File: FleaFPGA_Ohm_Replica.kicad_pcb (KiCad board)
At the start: 4 copper layers, 65 x 30 mm, 122 parts, among them J301 HDMI_C_1.3, J401 JTAG, J402 USB_B_Micro, J403 Conn_02x20, J404 Micro_SD_Card_Det2, J405 USB1, J406 USB2, U201 LFE5U-25F-6BGA256C, U401 FT230XQ, U402 MT48LC16M16A2, U403 MX25L1606, U404 TPD4E02B04DQA, U405 AP3417C, U406 AP3417C, U407 AP3417C, X401 XO32

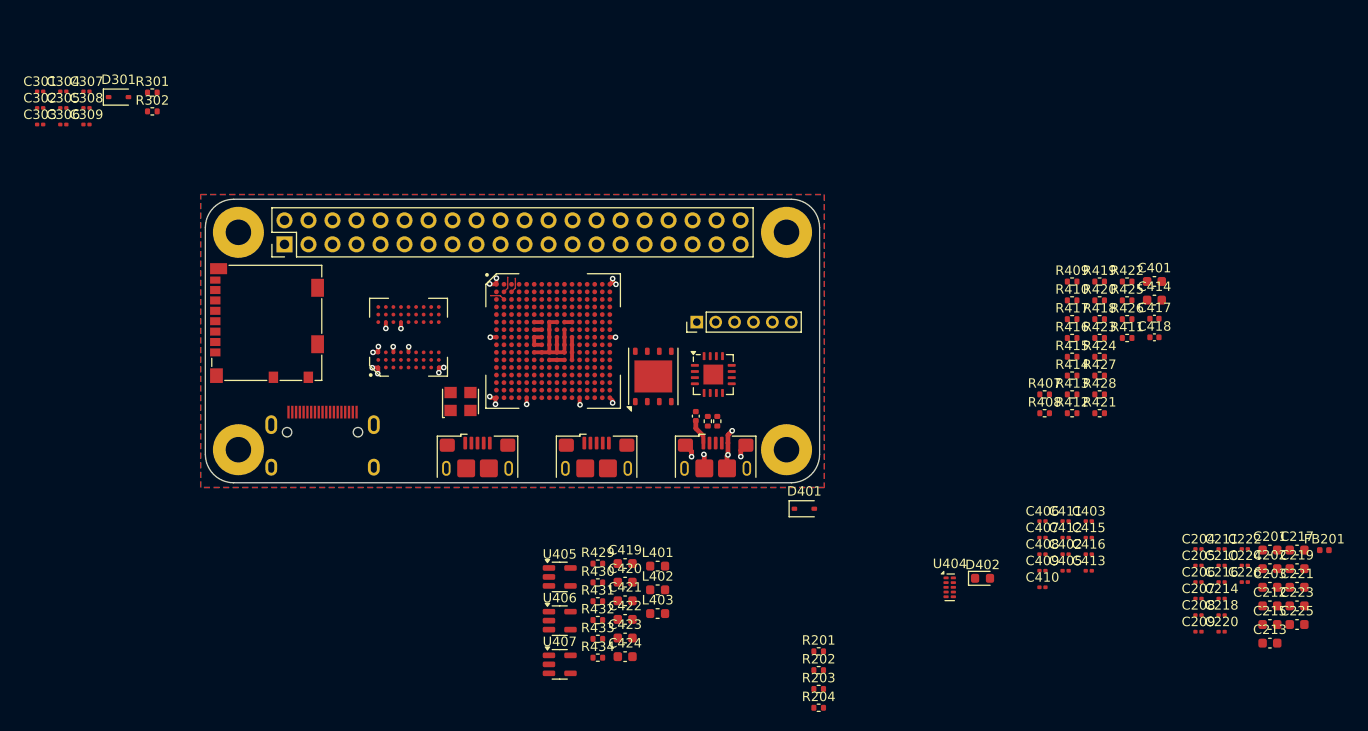
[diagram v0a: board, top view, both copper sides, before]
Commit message: Towards routing RAM
 - Moved the RAM to its own sheet
 - Use the ECP5 prefix to capture impedance controlled traces
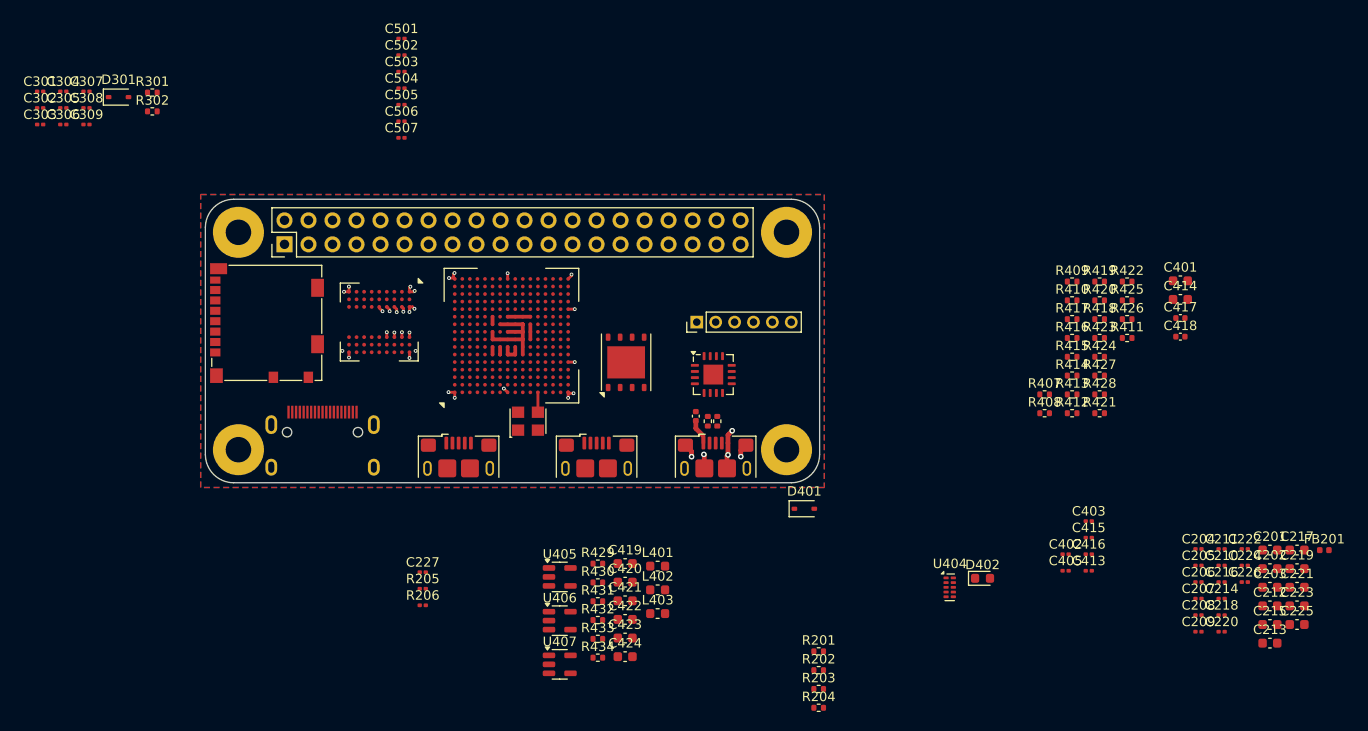
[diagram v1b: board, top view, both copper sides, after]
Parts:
- removed C406, C407, C408, C409, C410, C411, C412: 100n, Capacitor_SMD:C_0201_0603Metric
- removed U402: MT48LC16M16A2, Package_BGA_Extra:Micron_VFBGA-64_8.0x8.0mm_Layout9x9_P0.8mm
- added C227: 100n, Capacitor_SMD:C_0201_0603Metric, F.Cu at (123.0, 119.5)
- added C501: 100n, Capacitor_SMD:C_0201_0603Metric, F.Cu at (120.8, 63.0)
- added C502: 100n, Capacitor_SMD:C_0201_0603Metric, F.Cu at (120.8, 64.8)
- added C503: 100n, Capacitor_SMD:C_0201_0603Metric, F.Cu at (120.8, 66.5)
- added C504: 100n, Capacitor_SMD:C_0201_0603Metric, F.Cu at (120.8, 68.2)
- added C505: 100n, Capacitor_SMD:C_0201_0603Metric, F.Cu at (120.8, 70.0)
- added C506: 100n, Capacitor_SMD:C_0201_0603Metric, F.Cu at (120.8, 71.8)
- added C507: 100n, Capacitor_SMD:C_0201_0603Metric, F.Cu at (120.8, 73.5)
- added R205: 10k, Resistor_SMD:R_0201_0603Metric, F.Cu at (123.0, 121.2)
- added R206: 10k, Resistor_SMD:R_0201_0603Metric, F.Cu at (123.0, 123.0)
- added U501: MT48LC16M16A2, Package_BGA_Extra:Micron_VFBGA-64_8.0x8.0mm_Layout9x9_P0.8mm, F.Cu at (118.4, 93.0)
- moved X401 7.44 mm to (134.1, 103.5)
- moved U201 4.45 mm to (132.4, 94.4), turned to 90 degrees
- moved U403 3.24 mm to (144.5, 97.3)
- moved C401 2.75 mm to (203.2, 88.6)
- moved C414 2.75 mm to (203.2, 90.6)
- moved C417 2.75 mm to (203.2, 92.6)
- moved C418 2.75 mm to (203.2, 94.5)
- moved J406 2.00 mm to (126.8, 108.5)
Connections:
- U201 pad A10: unconnected-(U201A-PT42B-PadA10) -> /ECP5 FPGA/~{CAS}
- U201 pad A11: unconnected-(U201A-PT53A-PadA11) -> /ECP5 FPGA/BA1
- U201 pad A12: unconnected-(U201A-PT53B-PadA12) -> /ECP5 FPGA/BA0
- U201 pad A13: unconnected-(U201A-PT65A-PadA13) -> /ECP5 FPGA/CKE
- U201 pad A14: unconnected-(U201A-PT65B-PadA14) -> /ECP5 FPGA/CLK
- U201 pad A15: unconnected-(U201A-PT67B-PadA15) -> /ECP5 FPGA/UDQM
- U201 pad A9: unconnected-(U201A-PT42A-PadA9) -> /ECP5 FPGA/~{RAS}
- U201 pad L1: unconnected-(U201B-PL26A-PadL1) -> CK+
- U201 pad L2: unconnected-(U201B-PL26B-PadL2) -> CK-
- U201 pad M1: unconnected-(U201B-PL26C-PadM1) -> SYSCLK
- U201 pad N10: unconnected-(U201B-CFG_0-PadN10) -> GND
- U201 pad N9: unconnected-(U201B-CCLK-PadN9) -> ROM_CLK
- U201 pad P10: unconnected-(U201B-CFG_1-PadP10) -> Net-(U201B-CFG_1)
- U201 pad R10: unconnected-(U201B-CFG_2-PadR10) -> GND
- U201 pad R9: unconnected-(U201B-PROGRAMN-PadR9) -> Net-(U201B-PROGRAMN)
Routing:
- net +3V3: track 6.40 -> 9.76 mm, vias 0 -> 6
- net SYSCLK: track 0.00 -> 2.11 mm
- net unconnected-(U201B-PL2B-PadB2): track 1.71 -> 0.00 mm
- net unconnected-(U201A-PT4B-PadB3): track 1.60 -> 0.00 mm
- net unconnected-(U201B-PL5B-PadC2): track 1.56 -> 0.00 mm
- net GND: track 33.7 -> 32.5 mm, vias 26 -> 28
- removed copper zone on In1.Cu, net GND
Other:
- rule pad_to_mask_clearance: 0 -> 0.038

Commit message: First whole routing
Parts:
- removed C207, C208, C209, C220, C505, C506, C507: 100n, Capacitor_SMD:C_0201_0603Metric
- removed C215, C221, C225, C420, C422, C424: 10u, Capacitor_SMD:C_0603_1608Metric
- removed C421, C423: 4.7u, Capacitor_SMD:C_0603_1608Metric
- removed J401: JTAG, Connector_PinHeader_2.00mm:PinHeader_1x06_P2.00mm_Vertical
- removed J406: USB2, Connector_USB:USB_Micro-B_Amphenol_10118193-0001LF_Horizontal
- removed R201, R202, R203, R204: 4.7k, Resistor_SMD:R_0402_1005Metric
- removed R431: 320k, Resistor_SMD:R_0402_1005Metric
- removed R432, R434: 100k, Resistor_SMD:R_0402_1005Metric
- removed R433: 82k, Resistor_SMD:R_0402_1005Metric
- removed U407: AP3417C, Package_TO_SOT_SMD:SOT-23-5
- removed U501: MT48LC16M16A2, Package_BGA_Extra:Micron_VFBGA-64_8.0x8.0mm_Layout9x9_P0.8mm
- added C406: 4.7uF, Capacitor_SMD:C_0603_1608Metric, B.Cu at (163.4, 90.7)
- added C407: 22uF, Capacitor_SMD:C_0603_1608Metric, B.Cu at (158.8, 90.7)
- added C408: 4.7uF, Capacitor_SMD:C_0603_1608Metric, F.Cu at (163.6, 90.2)
- added C409: 22uF, Capacitor_SMD:C_0603_1608Metric, F.Cu at (159.1, 90.3)
- added C410: 4.7uF, Capacitor_SMD:C_0603_1608Metric, F.Cu at (155.2, 90.3)
- added C411: 10uF, Capacitor_SMD:C_0603_1608Metric, F.Cu at (150.5, 90.4)
- added C412: 22uF, Capacitor_SMD:C_0603_1608Metric, F.Cu at (157.6, 90.3)
- added D403: LED_Small, LED_SMD:LED_0603_1608Metric, F.Cu at (127.3, 106.2)
- added R401: 200k, Resistor_SMD:R_0402_1005Metric, B.Cu at (161.4, 87.9)
- added R402: 100k, Resistor_SMD:R_0402_1005Metric, B.Cu at (161.4, 88.9)
- added R403: 82.5k, Resistor_SMD:R_0402_1005Metric, F.Cu at (161.7, 93.2)
- added R405: 100k, Resistor_SMD:R_0402_1005Metric, F.Cu at (161.7, 92.1)
- added U1: TPD2EUSB30, Package_TO_SOT_SMD:Texas_DRT-3, F.Cu at (141.1, 101.1)
- added U2: ~, Package_BGA_Extra:FBGA-25_8x6mm_Layout5x5_P1mm, F.Cu at (119.5, 91.4)
- added U402: TLV62569DRL, Package_TO_SOT_SMD:SOT-563, B.Cu at (161.2, 90.7)
- C201, C202, C203, C212, C213, C217, C219, C223: footprint Capacitor_SMD:C_0603_1608Metric -> Capacitor_SMD:C_0402_1005Metric; moved to B.Cu
- C204, C205, C206, C210, C211, C214, C216, C218, C222, C224, C226, C227, C414, C415, FB201, R205, R206, R301, R302, R412, R413, R414, R415, R416, R417: moved to B.Cu
- C403: footprint Capacitor_SMD:C_0201_0603Metric -> Capacitor_SMD:C_0603_1608Metric; moved to B.Cu
- C417: footprint Capacitor_SMD:C_0402_1005Metric -> Capacitor_SMD:C_0603_1608Metric; moved to B.Cu
- C418: value 1u -> 1uF; moved to B.Cu
- C419: value 4.7u -> 1uF; footprint Capacitor_SMD:C_0603_1608Metric -> Capacitor_SMD:C_0402_1005Metric; moved to B.Cu
- C501, C502, C503: footprint Capacitor_SMD:C_0201_0603Metric -> Capacitor_SMD:C_0402_1005Metric; moved to B.Cu
- C504: value 100n -> 10u; footprint Capacitor_SMD:C_0201_0603Metric -> Capacitor_SMD:C_0402_1005Metric; moved to B.Cu
- L401: footprint Inductor_SMD:L_0603_1608Metric -> Inductor_SMD:L_0805_2012Metric; moved to B.Cu
- L402, L403: footprint Inductor_SMD:L_0603_1608Metric -> Inductor_SMD:L_0805_2012Metric
- R407: value 820 -> 450k
- R408: value 820 -> 100k
- R409: value 820 -> 330k; footprint Resistor_SMD:R_0402_1005Metric -> Resistor_SMD:R_0603_1608Metric; moved to B.Cu
- R410: value 820 -> 100k; moved to B.Cu
- R425: value 15k -> 22k; moved to B.Cu
- R426: value 15k -> 10k
- R427, R428: value 180 -> 10k
- R429: value 450k -> 10k
- R430: value 100k -> 180
- U403: footprint Package_SON:WSON-8-1EP_6x5mm_P1.27mm_EP3.4x4mm -> Package_SO_Extra:SOP-8-1EP_3.9x4.9mm_P1.27m_EP4.1x3.5mm
- U404: value TPD4E02B04DQA -> TLV62569DRL; footprint Package_SON:USON-10_2.5x1.0mm_P0.5mm -> Package_TO_SOT_SMD:SOT-563
- U405: value AP3417C -> TLV62569DRL; footprint Package_TO_SOT_SMD:SOT-23-5 -> Package_TO_SOT_SMD:SOT-563
- U406: value AP3417C -> TLV75801PDRV; footprint Package_TO_SOT_SMD:SOT-23-5 -> Package_SON:WSON-6-1EP_2x2mm_P0.65mm_EP1x1.6mm; moved to B.Cu
- moved C414 95.7 mm to (107.5, 92.4)
- moved C213 91.2 mm to (128.1, 92.7), turned to 180 degrees
- moved C415 91.0 mm to (105.6, 92.3), turned to 90 degrees
- moved C217 89.1 mm to (128.8, 96.4), turned to -135 degrees
- moved R413 89.0 mm to (103.7, 88.0), turned to -90 degrees
- moved R414 88.5 mm to (103.7, 90.1), turned to 90 degrees
- moved R417 88.3 mm to (103.5, 96.4), turned to -90 degrees
- moved R415 88.1 mm to (103.7, 93.5), turned to -90 degrees
- moved C403 87.4 mm to (110.2, 87.4), turned to 180 degrees
- moved C219 87.3 mm to (132.8, 91.2), turned to 180 degrees
- moved C202 87.1 mm to (129.2, 94.2), turned to -90 degrees
- moved R416 87.0 mm to (104.8, 95.3), turned to 90 degrees
- moved C223 85.9 mm to (133.6, 97.3), turned to -90 degrees
- moved R412 84.2 mm to (107.7, 97.0), turned to 180 degrees
- moved C201 83.6 mm to (131.3, 97.7)
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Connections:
- net /Peripherals/3V3OUT renamed /Peripherals and Power/3V3OUT
- net /Peripherals/USB_CONN_D+ renamed /Peripherals and Power/USB_CONN_D+
- net /Peripherals/USB_CONN_D- renamed /Peripherals and Power/USB_CONN_D-
- net /Peripherals/USB_D+ renamed /Peripherals and Power/USB_D+
- net /Peripherals/USB_D- renamed /Peripherals and Power/USB_D-
- net /Peripherals/VBUS renamed /Peripherals and Power/VBUS
- net Net-(C210-Pad1) renamed /ECP5 FPGA/VCCAUX
- net Net-(J301-CK+) renamed /Video out interface/CONN_HDMI_CLK+
- net Net-(J301-CK-) renamed /Video out interface/CONN_HDMI_CLK-
- net Net-(J301-D0+) renamed /Video out interface/CONN_HDMI_D0+
- net Net-(J301-D0-) renamed /Video out interface/CONN_HDMI_D0-
- net Net-(J301-D1+) renamed /Video out interface/CONN_HDMI_D1+
- net Net-(J301-D1-) renamed /Video out interface/CONN_HDMI_D1-
- net Net-(J301-D2+) renamed /Video out interface/CONN_HDMI_D2+
- net Net-(J301-D2-) renamed /Video out interface/CONN_HDMI_D2-
- net Net-(J301-SCL) renamed /Video out interface/HDMI_SCL
- net Net-(J301-SDA) renamed /Video out interface/HDMI_SDA
- net Net-(J405-D+) renamed /Peripherals and Power/USB1_CONN_DP
- net Net-(J405-D-) renamed /Peripherals and Power/USB1_CONN_DN
- net Net-(U201B-CFG_1) renamed /ECP5 FPGA/CFG_1
- net Net-(U201B-PROGRAMN) renamed /ECP5 FPGA/PROGRAMN
- net Net-(U403-HOLD#) renamed /Peripherals and Power/~{HOLD}
- net Net-(U403-WP#) renamed /Peripherals and Power/~{WP}
- C213 pad 1: +3V3 -> +1V8
- C214 pad 1: +3V3 -> +1V8
- C302 pad 1: CK- -> HDMI_CK-
- C303 pad 1: CK+ -> HDMI_CK+
- C304 pad 1: D0- -> HDMI_D0-
- C305 pad 1: D0+ -> HDMI_D0+
- C306 pad 1: D1- -> HDMI_D1-
- C307 pad 1: D1+ -> HDMI_D1+
- C308 pad 1: D2- -> HDMI_D2-
- C309 pad 1: D2+ -> HDMI_D2+
- C418 pad 1: +5V -> +3V3
- C419 pad 1: +5V -> +2V5
- C501 pad 1: +3V3 -> +1V8
- C502 pad 1: +3V3 -> +1V8
- C503 pad 1: +3V3 -> +1V8
- C504 pad 1: +3V3 -> +1V8
- L401 pad 1: Net-(U405-LX) -> /Peripherals and Power/SW1
- L401 pad 2: +3V3 -> +1V8
- L402 pad 1: Net-(U407-LX) -> /Peripherals and Power/SW2
- L403 pad 1: Net-(U406-LX) -> /Peripherals and Power/SW3
- L403 pad 2: +2V5 -> +3V3
- R407 pad 1: JTAG_TDO -> +3V3
- R407 pad 2: FTJTAG_TDO -> /Peripherals and Power/FB3
- R408 pad 1: JTAG_TDI -> /Peripherals and Power/FB3
- R408 pad 2: FJTAG_TDI -> GND
- R409 pad 1: JTAG_TMS -> +2V5
- R409 pad 2: FJTAG_TMS -> Net-(R409-Pad2)
- R410 pad 1: JTAG_TCK -> /Peripherals and Power/FB4
- R410 pad 2: FJTAG_TCK -> GND
- R423 pad 2: /Peripherals/USB1_CONN_DP -> USB1_DP
- R424 pad 2: /Peripherals/USB1_CONN_DN -> USB1_DN
- R425 pad 1: Net-(J406-D+) -> Net-(R409-Pad2)
- R425 pad 2: USB2_SEL -> /Peripherals and Power/FB4
- R426 pad 1: Net-(J406-D-) -> +3V3
- R426 pad 2: USB2_SEL -> JTAG_TDO
- R427 pad 1: Net-(J406-D+) -> +3V3
- R427 pad 2: /Peripherals/USB2_CONN_DP -> JTAG_TDI
- R428 pad 1: Net-(J406-D-) -> JTAG_TCK
- R428 pad 2: /Peripherals/USB2_CONN_DN -> GND
- R429 pad 2: Net-(U405-FB) -> JTAG_TMS
- R430 pad 1: Net-(U405-FB) -> GND
- R430 pad 2: GND -> Net-(D403-K)
- U201 pad A10: /ECP5 FPGA/~{CAS} -> unconnected-(U201A-PT42B-PadA10)
- U201 pad A11: /ECP5 FPGA/BA1 -> /ECP5 FPGA/DQ7
- U201 pad A12: /ECP5 FPGA/BA0 -> /ECP5 FPGA/DQ0
- U201 pad A13: /ECP5 FPGA/CKE -> /ECP5 FPGA/RWDS
- U201 pad A14: /ECP5 FPGA/CLK -> /ECP5 FPGA/DQ3
- U201 pad A15: /ECP5 FPGA/UDQM -> /ECP5 FPGA/DQ2
- U201 pad A2: unconnected-(U201A-PT4A-PadA2) -> HDMI_D2+
- U201 pad A3: unconnected-(U201A-PT6A-PadA3) -> HDMI_D1+
- U201 pad A4: unconnected-(U201A-PT6B-PadA4) -> HDMI_D1-
- U201 pad A5: unconnected-(U201A-PT18A-PadA5) -> HDMI_D0+
- U201 pad A6: unconnected-(U201A-PT18B-PadA6) -> HDMI_D0-
- U201 pad A7: unconnected-(U201A-PT29A-PadA7) -> HDMI_CK+
- U201 pad A8: unconnected-(U201A-PT29B-PadA8) -> HDMI_CK-
- U201 pad A9: /ECP5 FPGA/~{RAS} -> unconnected-(U201A-PT42A-PadA9)
- U201 pad B1: unconnected-(U201B-PL2A-PadB1) -> SD_DAT2
- U201 pad B11: unconnected-(U201A-PT49A-PadB11) -> /ECP5 FPGA/DQ1
- U201 pad B13: unconnected-(U201A-PT60A-PadB13) -> /ECP5 FPGA/DQ6
- U201 pad B14: unconnected-(U201A-PT67A-PadB14) -> /ECP5 FPGA/DQ4
- U201 pad B15: unconnected-(U201A-PR2B-PadB15) -> GPIO8
- U201 pad B16: unconnected-(U201A-PR2A-PadB16) -> GPIO9
- U201 pad B2: unconnected-(U201B-PL2B-PadB2) -> SD_CS
- U201 pad B3: unconnected-(U201A-PT4B-PadB3) -> HDMI_D2-
- U201 pad B8: unconnected-(U201A-PT35B-PadB8) -> /ECP5 FPGA/CK_P
- U201 pad C1: unconnected-(U201B-PL5A-PadC1) -> SD_DET
- U201 pad C13: unconnected-(U201A-PT60B-PadC13) -> /ECP5 FPGA/DQ5
- U201 pad C14: unconnected-(U201A-PR2C-PadC14) -> GPIO7
- U201 pad C15: unconnected-(U201A-PR5B-PadC15) -> GPIO0
- U201 pad C16: unconnected-(U201A-PR5A-PadC16) -> GPIO15
- U201 pad C2: unconnected-(U201B-PL5B-PadC2) -> SD_MOSI
- U201 pad C3: unconnected-(U201B-PL2C-PadC3) -> SD_CLK
- U201 pad C8: unconnected-(U201A-PT35A-PadC8) -> /ECP5 FPGA/CK_N
- U201 pad D1: unconnected-(U201B-PL8A-PadD1) -> USER_LED2
- U201 pad D13: unconnected-(U201A-PT62A-PadD13) -> /ECP5 FPGA/CS#
- U201 pad D14: unconnected-(U201A-PR2D-PadD14) -> GPIO16
- U201 pad D16: unconnected-(U201A-PR8A-PadD16) -> GPIO1
- U201 pad D3: unconnected-(U201B-PL2D-PadD3) -> SD_MISO
- U201 pad E1: unconnected-(U201B-PL11D-PadE1) -> USER_LED1
- U201 pad E13: unconnected-(U201A-PT62B-PadE13) -> /ECP5 FPGA/RESET#
- U201 pad E15: unconnected-(U201A-PR8B-PadE15) -> GPIO2
- U201 pad E16: unconnected-(U201A-PR11D-PadE16) -> GPIO3
- U201 pad E3: unconnected-(U201B-PL5C-PadE3) -> SD_DAT1
- U201 pad F10: +3V3 -> +1V8
- U201 pad F11: +3V3 -> +1V8
- U201 pad F15: unconnected-(U201A-PR11C-PadF15) -> GPIO4
- U201 pad F16: unconnected-(U201A-PR14A-PadF16) -> GPIO5
- U201 pad G16: unconnected-(U201A-PR20A-PadG16) -> GPIO12
- U201 pad M16: unconnected-(U201A-PR26C-PadM16) -> GPIO13
- U201 pad N13: unconnected-(U201A-PR38A-PadN13) -> SDA0
- U201 pad N14: unconnected-(U201A-PR35D-PadN14) -> GPIO6
- U201 pad N16: unconnected-(U201A-PR32A-PadN16) -> GPIO14
- U201 pad P14: unconnected-(U201A-PR38B-PadP14) -> SCL0
- U201 pad P15: unconnected-(U201A-PR32B-PadP15) -> GPIO11
- U201 pad P16: unconnected-(U201A-PR35A-PadP16) -> GPIO10
- U201 pad R13: unconnected-(U201A-PR41C-PadR13) -> GPIO25
- U201 pad R14: unconnected-(U201A-PR41B-PadR14) -> GPIO23
- U201 pad R15: unconnected-(U201A-PR38C-PadR15) -> GPIO26
- U201 pad R16: unconnected-(U201A-PR35B-PadR16) -> GPIO21
- U201 pad R5: unconnected-(U201B-PL44A-PadR5) -> USB1_DP
- U201 pad R8: unconnected-(U201B-PB13A-PadR8) -> ROM_MOSI
- U201 pad T13: unconnected-(U201A-PR44B-PadT13) -> GPIO29
- U201 pad T14: unconnected-(U201A-PR41D-PadT14) -> GPIO28
- U201 pad T15: unconnected-(U201A-PR38D-PadT15) -> GPIO22
- U201 pad T2: unconnected-(U201B-PL38D-PadT2) -> UART_RX
- U201 pad T3: unconnected-(U201B-PL41D-PadT3) -> USB1_SEL
- U201 pad T4: unconnected-(U201B-PL44B-PadT4) -> USB1_DN
- U201 pad T7: unconnected-(U201B-PB11A-PadT7) -> ROM_CS#
- U201 pad T8: unconnected-(U201B-PB11B-PadT8) -> ROM_MISO
- U401 pad 11: FTJTAG_TDO -> JTAG_TDO
- U401 pad 15: FJTAG_TMS -> JTAG_TMS
- U401 pad 16: FJTAG_TDI -> JTAG_TDI
- U401 pad 4: FJTAG_TCK -> JTAG_TCK
- U404 pad 1: /Peripherals/USB1_CONN_DN -> /Peripherals and Power/FB2
- U404 pad 2: /Peripherals/USB1_CONN_DP -> GND
- U404 pad 3: GND -> +5V
- U404 pad 4: /Peripherals/USB2_CONN_DN -> /Peripherals and Power/SW2
- U404 pad 5: /Peripherals/USB2_CONN_DP -> +5V
- U404 pad 6: USB2_DP -> unconnected-(U404-NC-Pad6)
- U405 pad 1: +5V -> /Peripherals and Power/FB3
- U405 pad 3: Net-(U405-LX) -> +5V
- U405 pad 4: Net-(U405-FB) -> /Peripherals and Power/SW3
- U406 pad 1: +3V3 -> +2V5
- U406 pad 2: GND -> /Peripherals and Power/FB4
- U406 pad 3: Net-(U406-LX) -> GND
- U406 pad 4: Net-(U406-FB) -> +3V3
- U406 pad 5: +3V3 -> unconnected-(U406-DNC-Pad5)
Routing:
- net GND: track 32.5 -> 143.3 mm, vias 28 -> 71
- net +5V: track 0.00 -> 100.8 mm, vias 0 -> 9
- net +1V8: track 0.00 -> 65.4 mm, vias 0 -> 6
- net +3V3: track 9.76 -> 70.9 mm, vias 6 -> 23
- net JTAG_TDO: track 0.00 -> 41.3 mm, vias 0 -> 2
- net SD_DAT1: track 0.00 -> 33.1 mm, vias 0 -> 2
- net JTAG_TCK: track 0.00 -> 32.3 mm, vias 0 -> 2
- net SD_MISO: track 0.00 -> 31.9 mm, vias 0 -> 2
- net SD_CLK: track 0.00 -> 30.7 mm, vias 0 -> 2
- net JTAG_TDI: track 0.00 -> 30.2 mm, vias 0 -> 2
- net SD_DAT2: track 0.00 -> 30.2 mm, vias 0 -> 2
- net JTAG_TMS: track 0.00 -> 30.2 mm, vias 0 -> 2
- net SD_MOSI: track 0.00 -> 29.6 mm, vias 0 -> 2
- net SD_CS: track 0.00 -> 28.8 mm, vias 0 -> 2
- net SD_DET: track 0.00 -> 26.7 mm, vias 0 -> 2
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- added copper zone on F.Cu, net +1V1
- added copper zone on In2.Cu, net +1V1
- added copper zone on B.Cu, net +1V8
- added copper zone on F.Cu, net +3V3
- added copper zone on In2.Cu, net +3V3
- added copper zone on B.Cu, net +5V
- added copper zone on F.Cu, net +5V
- added copper zone on In2.Cu, net +5V
- added copper zone on B.Cu, net /Peripherals and Power/SW1
- added copper zone on F.Cu, net /Peripherals and Power/SW2
- added copper zone on F.Cu, net /Peripherals and Power/SW3
- added copper zone on In1.Cu, net GND

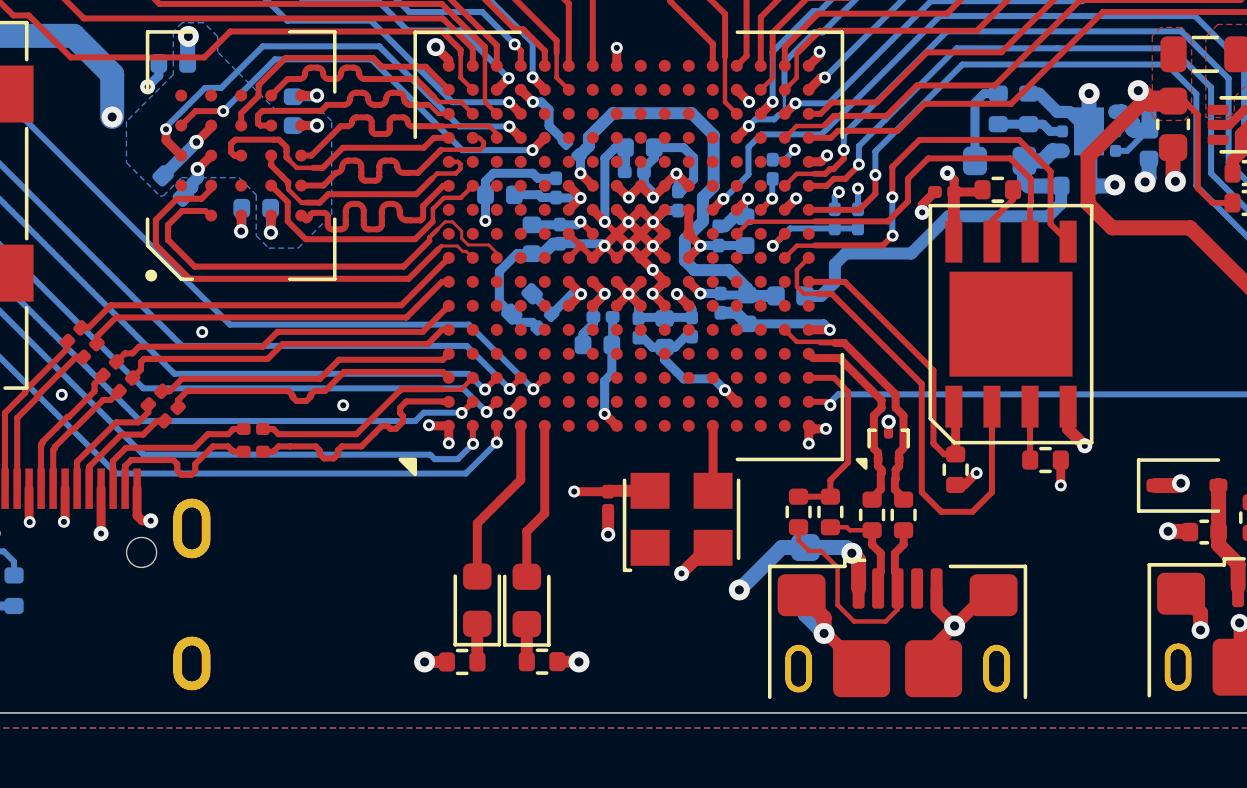
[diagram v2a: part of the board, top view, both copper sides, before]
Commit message: Update some component values and complete MPN for BOM
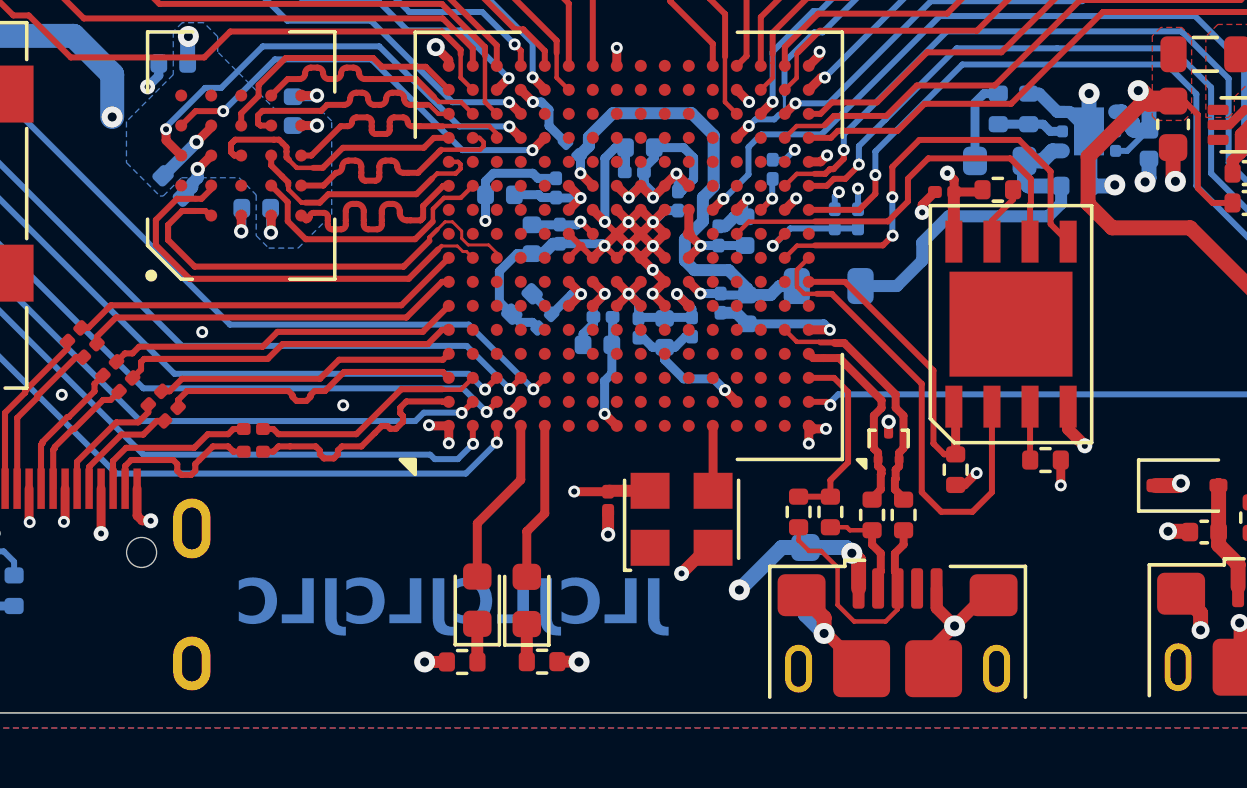
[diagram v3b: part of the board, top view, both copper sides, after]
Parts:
- C201, C202, C203, C212, C213, C217, C219, C223, C414, C504: value 10u -> 10uF
- C204, C205, C206, C210, C211, C214, C216, C218, C222, C224, C226, C227, C301, C302, C303, C304, C305, C306, C307, C308, C309, C402, C403, C404, C405, C413, C415, C416, C501, C502, C503: value 100n -> 100nF
- C401: value 4.7u -> 4.7uF
- C417: value 1u -> 1uF
- D301: value NSR0530HT1G -> 1N5819WS
- D401: value BAT60JFILM -> 1N5819WS
- FB201: value 120 @ 100MHz -> 100 @ 100MHz; footprint Inductor_SMD:L_0402_1005Metric -> Inductor_SMD:L_0805_2012Metric
- J301: value HDMI_C_1.3 -> GT-HD005A-CGNG0
- J402: value USB_B_Micro -> Amph 10118193-0001LF
- J404: value Micro_SD_Card_Det2 -> Molex 1040310811
- J405: value USB1 -> Amph 10118193-0001LF
- U2: value ~ -> W958D8NBYA5I
- moved FB201 1.31 mm to (139.1, 95.8)
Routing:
- net +2V5: track 14.1 -> 12.1 mm
- net /ECP5 FPGA/VCCAUX: track 17.0 -> 17.8 mm
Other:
- board text added: "JLCJLCJLCJLC"

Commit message: Last minute changes before sending to JLCPCB
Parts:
- U2: footprint Package_BGA_Extra:FBGA-25_8x6mm_Layout5x5_P1mm -> Package_BGA_Extra:FBGA-25_8x6mm_Layout5x6_P1mm

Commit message: Minor fixes
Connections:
- net UART_RX renamed UART_TX
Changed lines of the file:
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@@
 	(net 188 "CK-")
 	(net 189 "CK+")
-	(net 190 "UART_RX")
+	(net 190 "UART_TX")
 	(net 191 "/Video out interface/CONN_HDMI_CLK+")
 	(net 192 "HDMI_D2+")
@@
 			(layers "F.Cu" "F.Paste" "F.Mask")
 			(roundrect_rratio 0.25)
-			(net 190 "UART_RX")
+			(net 190 "UART_TX")
 			(pinfunction "RXD")
 			(pintype "input")
@@
 			(size 0.4 0.4)
 			(layers "F.Cu" "F.Paste" "F.Mask")
-			(net 190 "UART_RX")
+			(net 190 "UART_TX")
 			(pinfunction "PL38D")
 			(pintype "bidirectional")
